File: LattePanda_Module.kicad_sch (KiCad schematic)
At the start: 10 parts, among them J1 Conn_01x03_Pin

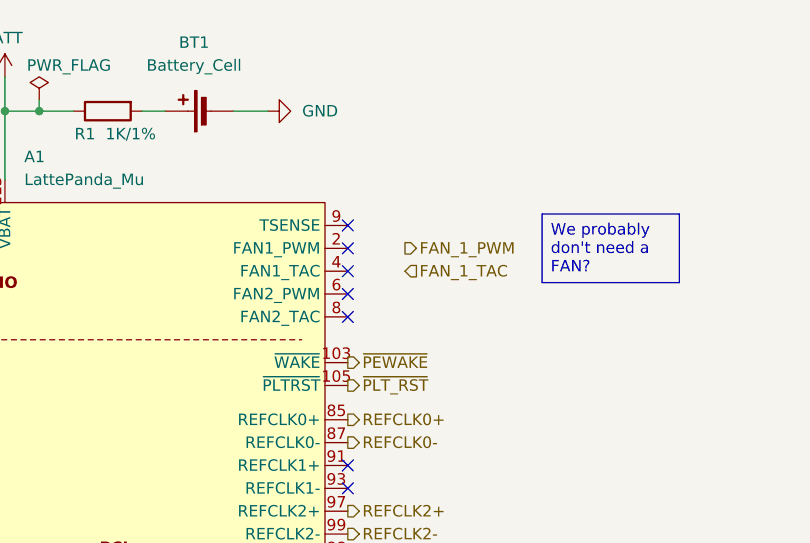
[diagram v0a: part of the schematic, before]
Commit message: finished schematic draft and started placing components
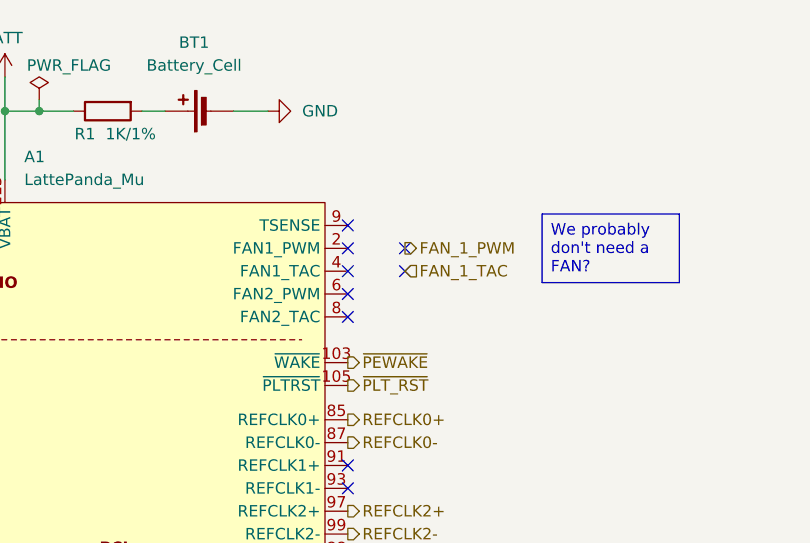
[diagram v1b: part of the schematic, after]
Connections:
- no-connect marks 77 -> 79
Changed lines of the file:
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@@
+	)
+	(no_connect
+		(at 331.47 69.85)
 	)
 	(no_connect
@@
 	)
 	(no_connect
+		(at 331.47 72.39)
+	)
+	(no_connect

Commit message: commit before removing duplicated glasgow
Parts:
- removed R78, R79: 10K/1%, symbol Device:R
- BT1: footprint (none) -> A_HDJ_Library:Battery_Holder_CR1220_S8411-45R
- J1: footprint (none) -> A_HDJ_Library:PinHeader_1x03_P2.54mm_Vertical
- R1: renamed from R76; footprint (none) -> A_DFRobot:R_0603_1608Metric
- R2: renamed from R77; footprint (none) -> A_DFRobot:R_0603_1608Metric
- R3: renamed from R1; footprint (none) -> A_DFRobot:R_0603_1608Metric
- R4: renamed from R2; footprint (none) -> A_DFRobot:R_0603_1608Metric
- TP1: renamed from TP7; footprint (none) -> TestPoint:TestPoint_Pad_2.5x2.5mm
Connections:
- net CLKREQ4: now reaches A1.102 (~{CLKREQ4})
- net CLKREQ3: now reaches A1.100 (~{CLKREQ3})
- net USB_2_P4+: now reaches A1.70 (USB2_P4+)
- net USB_2_P4-: now reaches A1.72 (USB2_P4-)
- net USB_2_P8+: now reaches A1.82 (USB2_P8+)
- net USB_2_P8-: now reaches A1.84 (USB2_P8-)
- net REFCLK1+: now reaches A1.91 (REFCLK1+)
- net REFCLK1-: now reaches A1.93 (REFCLK1-)
- no-connect marks 79 -> 73
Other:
- note added: "DDI/TCP functions are defined by the BIOS firmware, Cannot be changed in BIOS menu. Before starting design, you should choose one of the available BIOS configurations on: https://github.com/LattePandaTeam/LattePanda-Mu The default functions are defined as follows: - DDIA: eDP 1.4b (the 40Pin connector on the Mu) - DDIB: HDMI 2.0 - TCP0: HDMI 2.0 - TCP1: USB TypeC (need external PD controller)"
- note added: "HSIO functions are defined by the BIOS firmware, Cannot be changed in BIOS menu. Before starting design, you should choose one of the available BIOS configurations on: https://github.com/LattePandaTeam/LattePanda-Mu Or contact techsupport for custom your BIOS The default functions are defined as follows: - HSIO0: USB3.2 10Gbps - HSIO1: USB3.2 10Gbps - HSIO2: PCIe 3.0 x1 - HSIO3: PCIe 3.0 x1 - HSI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"
- note added: "State Signal - PWR_LED/PSON: - S0 (Working): HIGH - S3 (Slpeeping): LOW - S4 (Hibernation): LOW - S5 (Soft Off): LOW - SLS_S4_N: - S0 (Working): HIGH - S3 (Slpeeping): HIGH - S4 (Hibernation): LOW - S5 (Soft Off): LOW"

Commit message: is this a differential pair?
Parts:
- BT1: Buy_Link (none) -> https://item.szlcsc.com/1049689.html; DF_Comment (none) -> CR1220电池底座_BS-12-B3AA003
- J1: DF_Comment (none) -> 2.54红色单排排针-3P
- R1, R2, R3, R4: Buy_Link (none) -> https://item.szlcsc.com/8530937.html; DF_Comment (none) -> 0603贴片自恢复保险丝0.05A-6V_0603L005-6AR; SCH_Show_Footprint (none) -> R0805
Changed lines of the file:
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@@
+			)
+		)
+		(property "Buy_Link" "https://item.szlcsc.com/8530937.html"
+			(at 233.68 290.83 0)
+			(effects
+				(font
+					(size 1.27 1.27)
+				)
+				(hide yes)
+			)
+		)
+		(property "DF_Comment" "0603贴片自恢复保险丝0.05A-6V_0603L005-6AR"
+			(at 233.68 290.83 0)
+			(effects
+				(font
+					(size 1.27 1.27)
+				)
+				(hide yes)
+			)
+		)
+		(property "Field-1" ""
+			(at 233.68 290.83 0)
+			(effects
+				(font
+					(size 1.27 1.27)
+				)
+				(hide yes)
+			)
+		)
+		(property "SCH_Show_Footprint" "R0805"
+			(at 233.68 290.83 0)
+			(effects
+				(font
+					(size 1.27 1.27)
+				)
+				(hide yes)
 			)
 		)
@@
 			)
 		)
+		(property "DF_Comment" "2.54红色单排排针-3P"
+			(at 220.98 72.39 0)
+			(effects
+				(font
+					(size 1.27 1.27)
+				)
+				(hide yes)
+			)
+		)
+		(property "Field-1" ""
+			(at 220.98 72.39 0)
+			(effects
+				(font
+					(size 1.27 1.27)
+				)
+				(hide yes)
+			)
+		)
 		(pin "2"
 		)
@@
 			)
 		)
+		(property "Buy_Link" "https://item.szlcsc.com/8530937.html"
+			(at 233.68 252.73 0)
+			(effects
+				(font
+					(size 1.27 1.27)
+				)
+				(hide yes)
+			)
+		)
+		(property "DF_Comment" "0603贴片自恢复保险丝0.05A-6V_0603L005-6AR"
+			(at 233.68 252.73 0)
+			(effects
+				(font
+					(size 1.27 1.27)
+				)
+				(hide yes)
+			)
+		)
+		(property "Field-1" ""
+			(at 233.68 252.73 0)
+			(effects
+				(font
+					(size 1.27 1.27)
+				)
+				(hide yes)
+			)
+		)
+		(property "SCH_Show_Footprint" "R0805"
+			(at 233.68 252.73 0)
+			(effects
+				(font
+					(size 1.27 1.27)
+				)
+				(hide yes)
+			)
+		)
 		(pin "2"
 		)
@@
 			)
 		)
+		(property "Buy_Link" "https://item.szlcsc.com/8530937.html"
+			(at 298.45 54.61 0)
+			(effects
+				(font
+					(size 1.27 1.27)
+				)
+				(hide yes)
+			)
+		)
+		(property "DF_Comment" "0603贴片自恢复保险丝0.05A-6V_0603L005-6AR"
+			(at 298.45 54.61 0)
+			(effects
+				(font
+					(size 1.27 1.27)
+				)
+				(hide yes)
+			)
+		)
+		(property "Field-1" ""
+			(at 298.45 54.61 0)
+			(effects
+				(font
+					(size 1.27 1.27)
+				)
+				(hide yes)
+			)
+		)
+		(property "SCH_Show_Footprint" "R0805"
+			(at 298.45 54.61 0)
+			(effects
+				(font
+					(size 1.27 1.27)
+				)
+				(hide yes)
+			)
+		)
 		(pin "2"
 		)
@@
 			)
 		)
+		(property "Buy_Link" "https://item.szlcsc.com/1049689.html"
+			(at 309.88 54.61 0)
+			(effects
+				(font
+					(size 1.27 1.27)
+				)
+				(hide yes)
+			)
+		)
+		(property "DF_Comment" "CR1220电池底座_BS-12-B3AA003"
+			(at 309.88 54.61 0)
+			(effects
+				(font
+					(size 1.27 1.27)
+				)
+				(hide yes)
+			)
+		)
+		(property "Field-1" ""
+			(at 309.88 54.61 0)
+			(effects
+				(font
+					(size 1.27 1.27)
+				)
+				(hide yes)
+			)
+		)
+		(property "SCH_Show_Footprint" ""
+			(at 309.88 54.61 0)
+			(effects
+				(font
+					(size 1.27 1.27)
+				)
+				(hide yes)
+			)
+		)
 		(pin "2"
 		)
@@
 			(at 332.74 262.89 0)
 			(effects
+				(font
+					(size 1.27 1.27)
+				)
+				(hide yes)
+			)
+		)
+		(property "Buy_Link" "https://item.szlcsc.com/8530937.html"
+			(at 332.74 262.89 0)
+			(effects
+				(font
+					(size 1.27 1.27)
+				)
+				(hide yes)
+			)
+		)
+		(property "DF_Comment" "0603贴片自恢复保险丝0.05A-6V_0603L005-6AR"
+			(at 332.74 262.89 0)
+			(effects
+				(font
+					(size 1.27 1.27)
+				)
+				(hide yes)
+			)
+		)
+		(property "Field-1" ""
+			(at 332.74 262.89 0)
+			(effects
+				(font
+					(size 1.27 1.27)
+				)
+				(hide yes)
+			)
+		)
+		(property "SCH_Show_Footprint" "R0805"
+			(at 332.74 262.89 0)
+			(effects

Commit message: power finished started diff pairs
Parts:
- BT1: footprint A_HDJ_Library:Battery_Holder_CR1220_S8411-45R -> A_DFRobot:Battery_Holder_CR1220_S8411-45R
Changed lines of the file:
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@@
 			)
 		)
-		(property "Footprint" "A_HDJ_Library:Battery_Holder_CR1220_S8411-45R"
+		(property "Footprint" "A_DFRobot:Battery_Holder_CR1220_S8411-45R"
 			(at 308.356 54.61 90)
 			(hide yes)

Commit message: all power, diff pairs done, all components placed (final spot?) just some small wires left to route
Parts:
- removed R4: 10K/1%, A_DFRobot:R_0603_1608Metric, symbol Device:R
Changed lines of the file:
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@@
 	)
 	(junction
-		(at 327.66 262.89)
-		(diameter 0)
-		(color 0 0 0 0)
-	)
-	(junction
 		(at 284.48 334.01)
 		(diameter 0)
@@
 	(wire
 		(pts
-			(xy 336.55 262.89) (xy 340.36 262.89)
-		)
-		(stroke
-			(width 0)
-			(type default)
-		)
-	)
-	(wire
-		(pts
 			(xy 283.21 50.8) (xy 283.21 62.23)
 		)
@@
 	(wire
 		(pts
-			(xy 327.66 262.89) (xy 328.93 262.89)
-		)
-		(stroke
-			(width 0)
-			(type default)
-		)
-	)
-	(wire
-		(pts
 			(xy 226.06 252.73) (xy 226.06 254)
 		)
@@
 	)
 	(symbol
-		(lib_id "power:+3V3")
-		(at 340.36 262.89 270)
-		(unit 1)
-		(body_style 1)
-		(exclude_from_sim no)
-		(in_bom yes)
-		(on_board yes)
-		(in_pos_files yes)
-		(dnp no)
-		(fields_autoplaced yes)
-		(property "Reference" "#PWR012"
-			(at 336.55 262.89 0)
-			(hide yes)
-			(show_name no)
-			(do_not_autoplace no)
-			(effects
-				(font
-					(size 1.27 1.27)
-				)
-			)
-		)
-		(property "Value" "VPullup"
-			(at 344.17 262.8899 90)
-			(show_name no)
-			(do_not_autoplace no)
-			(effects
-				(font
-					(size 1.27 1.27)
-				)
-				(justify left)
-			)
-		)
-		(property "Footprint" ""
-			(at 340.36 262.89 0)
-			(hide yes)
-			(show_name no)
-			(do_not_autoplace no)
-			(effects
-				(font
-					(size 1.27 1.27)
-				)
-			)
-		)
-		(property "Datasheet" ""
-			(at 340.36 262.89 0)
-			(hide yes)
-			(show_name no)
-			(do_not_autoplace no)
-			(effects
-				(font
-					(size 1.27 1.27)
-				)
-			)
-		)
-		(property "Description" "Power symbol creates a global label with name \"+3V3\""
-			(at 340.36 262.89 0)
-			(hide yes)
-			(show_name no)
-			(do_not_autoplace no)
-			(effects
-				(font
-					(size 1.27 1.27)
-				)
-			)
-		)
-		(pin "1"
-		)
-		(instances
-			(project "microcyber"
-				(path "/7ac319af-771c-4997-a005-b73a4a9b44ab/64b35e3f-e07a-4023-bcd4-186bab824450"
-					(reference "#PWR012")
-					(unit 1)
-				)
-			)
-		)
-	)
-	(symbol
 		(lib_id "Connector:Conn_01x03_Pin")
 		(at 220.98 72.39 270)
@@
 					(unit 1)
 				)
-			)
-		)
-	)
-	(symbol
-		(lib_id "Device:R")
-		(at 332.74 262.89 270)
-		(mirror x)
-		(unit 1)
-		(body_style 1)
-		(exclude_from_sim no)
-		(in_bom yes)
-		(on_board yes)
-		(in_pos_files yes)
-		(dnp no)
-		(property "Reference" "R4"
-			(at 337.566 265.176 90)
-			(show_name no)
-			(do_not_autoplace no)
-			(effects
-				(font
-					(size 1.27 1.27)
-				)
-			)
-		)
-		(property "Value" "10K/1%"
-			(at 332.232 265.176 90)
-			(show_name no)
-			(do_not_autoplace no)
-			(effects
-				(font
-					(size 1.27 1.27)
-				)
-			)
-		)
-		(property "Footprint" "A_DFRobot:R_0603_1608Metric"
-			(at 332.74 264.668 90)
-			(hide yes)
-			(show_name no)
-			(do_not_autoplace no)
-			(effects
-				(font
-					(size 1.27 1.27)
-				)
-			)
-		)
-		(property "Datasheet" ""
-			(at 332.74 262.89 0)
-			(hide yes)
-			(show_name no)
-			(do_not_autoplace no)
-			(effects
-				(font
-					(size 1.27 1.27)
-				)
-			)
-		)
-		(property "Description" "Resistor"
-			(at 332.74 262.89 0)
-			(hide yes)
-			(show_name no)
-			(do_not_autoplace no)
-			(effects
-				(font
-					(size 1.27 1.27)
-				)
-			)
-		)
-		(property "Buy_Link" "https://item.szlcsc.com/8530937.html"
-			(at 332.74 262.89 0)
-			(hide yes)
-			(show_name no)
-			(do_not_autoplace no)
-			(effects
-				(font
-					(size 1.27 1.27)
-				)
-			)
-		)
-		(property "DF_Comment" "0603贴片自恢复保险丝0.05A-6V_0603L005-6AR"
-			(at 332.74 262.89 0)
-			(hide yes)
-			(show_name no)
-			(do_not_autoplace no)
-			(effects
-				(font
-					(size 1.27 1.27)
-				)
-			)
-		)
-		(property "Field-1" ""
-			(at 332.74 262.89 0)
-			(hide yes)
-			(show_name no)
-			(do_not_autoplace no)
-			(effects
-				(font
-					(size 1.27 1.27)
-				)
-			)
-		)
-		(property "SCH_Show_Footprint" "R0805"
-			(at 332.74 262.89 0)
-			(hide yes)
-			(show_name no)
-			(do_not_autoplace no)
-			(effects
-				(font
-					(size 1.27 1.27)
-				)
-			)
-		)
-		(pin "2"
-		)
-		(pin "1"
-		)
-		(instances
-			(project "microcyber"
-				(path "/7ac319af-771c-4997-a005-b73a4a9b44ab/64b35e3f-e07a-4023-bcd4-186bab824450"
-					(reference "R4")
-					(unit 1)
-				)

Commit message: V4 done ???
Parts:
- added H12, H13: MountingHole_M2.0, MountingHole:MountingHole_2.7mm_Pad_TopOnly, symbol Mechanical:MountingHole_Pad
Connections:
- net GND: now also H12.1, H13.1
- net HSIO_0_RX+: now also A1.18 (HSIO0_RX-); no longer A1.16 (HSIO0_RX+)
- net HSIO_0_RX-: now also A1.16 (HSIO0_RX+); no longer A1.18 (HSIO0_RX-)
- net HSIO_0_TX+: now also A1.15 (HSIO0_TX-); no longer A1.13 (HSIO0_TX+)
- net HSIO_0_TX-: now also A1.13 (HSIO0_TX+); no longer A1.15 (HSIO0_TX-)
- net HSIO_11_RX+: now also A1.60 (HSIO11_RX-); no longer A1.58 (HSIO11_RX+)
- net HSIO_11_RX-: now also A1.58 (HSIO11_RX+); no longer A1.60 (HSIO11_RX-)
- net HSIO_11_TX+: now also A1.57 (HSIO11_TX-); no longer A1.55 (HSIO11_TX+)
- net HSIO_11_TX-: now also A1.55 (HSIO11_TX+); no longer A1.57 (HSIO11_TX-)
- net HSIO_9_RX+: now also A1.48 (HSIO9_RX-); no longer A1.46 (HSIO9_RX+)
- net HSIO_9_RX-: now also A1.46 (HSIO9_RX+); no longer A1.48 (HSIO9_RX-)
- net HSIO_9_TX+: now also A1.45 (HSIO9_TX-); no longer A1.43 (HSIO9_TX+)
- net HSIO_9_TX-: now also A1.43 (HSIO9_TX+); no longer A1.45 (HSIO9_TX-)
- net REFCLK0+: now also A1.87 (REFCLK0-); no longer A1.85 (REFCLK0+)
- net REFCLK0-: now also A1.85 (REFCLK0+); no longer A1.87 (REFCLK0-)
- net REFCLK1+: now also A1.93 (REFCLK1-); no longer A1.91 (REFCLK1+)
- net REFCLK1-: now also A1.91 (REFCLK1+); no longer A1.93 (REFCLK1-)
- net REFCLK3+: now also A1.90 (REFCLK3-); no longer A1.88 (REFCLK3+)
- net REFCLK3-: now also A1.88 (REFCLK3+); no longer A1.90 (REFCLK3-)

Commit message: more fixes, tweaks, pretty
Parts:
- added R13, R14, R4: 0, A_DFRobot:R_0603_1608Metric, symbol Device:R
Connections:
- net SMB_ALERT: now reaches A1.104 (~{SMB_ALERT})
- net SMB_CLK: now reaches A1.106 (SMB_CLK)
- net SMB_DATA: now reaches A1.108 (SMB_DATA)
- net USB_2_P6_PD+: now reaches A1.112 (USB2_P6+)
- net USB_2_P6_PD-: now reaches A1.114 (USB2_P6-)
- net at A1.125 (GPP_B11): now also R14.1
- net at A1.145 (SML1_DATA): now also R4.1
- net at A1.147 (SML1_CLK): now also R13.1
- new net PMCALERT: R14.2
- new net SML1CLK: R13.2
- new net SML1DATA: R4.2
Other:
- note added: "also for smlink"
- note added: "smlink is for me to negotiate dp"
